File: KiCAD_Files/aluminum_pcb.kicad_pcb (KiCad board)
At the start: 2 copper layers, 160 x 133.9 mm, 189 parts, among them J1 Conn_01x01, J2 Conn_01x01, J3 Conn_01x01, J5 Conn_01x01, J8 Conn_01x01, K1 HF140FF/012-2HSWTF, Q11 NMOS, T1 Transformer_1P_1S, T2 Transformer_1P_1S, U1 INA240A1PW, U2 INA240A1PWR, U3 UCC27282DRC, U4 UCC27282DRC, U401 AMC1311BDWVR, U402 MCP6486UT-E/LT, U5 AMC1301DWR, U501 AMC1301DWR, U502 MCP6486UT-E/LT, U701 MCP6486UT-E/LT, U8 MCP6486UT-E/LT, U801 ISO7720DWV, U802 ISO7720DWV, U803 ISO7330C

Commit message: First routing pass complete.
Signed-off-by: Jean Alinei <jean.alinei@owntech.org>
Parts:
- removed C2, C4: C_Small, Capacitor_SMD:C_0805_2012Metric
- removed C5002: 470nF, Footprints:C_0805_2012Metric
- removed C5005: 4.7uF, Footprints:C_1210_3225Metric
- removed HS1, HS13, HS14, HS15, HS16, HS17, HS18, HS2, HS6, HS7, HS8: 5x3mm pad 3mm high, Footprints:BTC-533-ZN01
- removed L5001: 10uH, Inductor_SMD:L_1210_3225Metric
- added C101: 4.7uF, Capacitor_SMD:C_0805_2012Metric, F.Cu at (196.1, 88.4)
- added C102: 4.7uF, Capacitor_SMD:C_0805_2012Metric, F.Cu at (200.1, 59.5)
- added C103: 10µF, Capacitor_SMD:C_1206_3216Metric, F.Cu at (97.6, 148.1)
- added C104: C, Capacitor_SMD:C_1206_3216Metric, F.Cu at (97.6, 150.4)
- added C105: C, Capacitor_SMD:C_1206_3216Metric, F.Cu at (97.6, 152.7)
- added C106: C, Capacitor_SMD:C_1206_3216Metric, F.Cu at (97.6, 155.0)
- added C107: C, Capacitor_SMD:C_1206_3216Metric, F.Cu at (107.0, 155.0)
- added C108: C, Capacitor_SMD:C_1206_3216Metric, F.Cu at (107.0, 152.7)
- added C109: C, Capacitor_SMD:C_1206_3216Metric, F.Cu at (107.0, 150.4)
- added C110: 10µF, Capacitor_SMD:C_1206_3216Metric, F.Cu at (107.0, 148.1)
- added C111: 47uF, Capacitor_SMD:C_Elec_10x10.2, F.Cu at (96.6, 137.1)
- added C112: 47uH, Capacitor_SMD:C_Elec_10x10.2, F.Cu at (96.2, 165.2)
- added C113: ?nF, Capacitor_THT:C_Rect_L16.5mm_W7.0mm_P15.00mm_MKT, F.Cu at (142.3, 72.4)
- added C114: 1nF, Capacitor_SMD:C_1210_3225Metric, F.Cu at (210.0, 71.1)
- added C115: 1nF, Capacitor_SMD:C_1210_3225Metric, F.Cu at (210.0, 76.4)
- added C701: 1nF, Capacitor_SMD:C_0805_2012Metric, B.Cu at (86.6, 136.6)
- added C703: 100nF, Capacitor_SMD:C_0805_2012Metric, F.Cu at (137.6, 115.0)
- added C704: 22uF, Capacitor_SMD:C_1210_3225Metric, F.Cu at (123.3, 111.8)
- added C705: 33pF, Capacitor_SMD:C_0805_2012Metric, F.Cu at (134.3, 122.3)
- added C706: 10uF, Capacitor_SMD:C_0805_2012Metric, F.Cu at (120.3, 108.3)
- added C707: 100nF, Capacitor_SMD:C_0805_2012Metric, F.Cu at (117.1, 104.3)
- added C708: 47uF, Capacitor_SMD:C_1206_3216Metric, F.Cu at (119.4, 102.8)
- added C709: 10uF, Capacitor_SMD:C_0805_2012Metric, F.Cu at (140.2, 101.1)
- added C710: 10uF, Capacitor_SMD:C_0805_2012Metric, F.Cu at (109.9, 100.0)
- added C711: 10uF, Capacitor_SMD:C_0805_2012Metric, F.Cu at (143.2, 104.2)
- added C712: 10uF, Capacitor_SMD:C_0805_2012Metric, F.Cu at (111.1, 97.2)
- added C713: 100nF, Capacitor_SMD:C_0603_1608Metric, F.Cu at (146.5, 105.5)
- added C714: 100nF, Capacitor_SMD:C_0603_1608Metric, F.Cu at (109.3, 97.0)
- added C715: 10uF, Capacitor_SMD:C_0805_2012Metric, F.Cu at (161.6, 101.6)
- added C716: 10uF, Capacitor_SMD:C_0805_2012Metric, F.Cu at (106.1, 79.2)
- added C717: 470nF, Footprints:C_0805_2012Metric, F.Cu at (123.9, 115.8)
- added C718: 4.7uF, Footprints:C_1210_3225Metric, F.Cu at (126.6, 115.6)
- added C807: 100nF, Capacitor_SMD:C_0805_2012Metric, F.Cu at (200.4, 89.2)
- added C808: 100nF, Capacitor_SMD:C_0805_2012Metric, F.Cu at (199.1, 54.6)
- added C809: 100nF, Capacitor_SMD:C_0805_2012Metric, F.Cu at (214.3, 88.0)
- added D101: D, Footprints:D_SOD-123, F.Cu at (208.5, 87.6)
- added D102: D, Footprints:D_SOD-123, F.Cu at (207.7, 59.5)
- added D701: PMEG3010, Diode_SMD:D_SOD-323F, F.Cu at (161.5, 97.0)
- added D702: PMEG3010, Diode_SMD:D_SOD-323F, F.Cu at (161.4, 103.8)
- added D703: PMEG3010, Diode_SMD:D_SOD-323F, F.Cu at (103.6, 79.4)
- added D704: PMEG3010, Diode_SMD:D_SOD-323F, F.Cu at (110.3, 79.3)
- added F101: 2.5A, Footprints:FUSE-TH_L8.4-W4.1-P5.08-D0.6, F.Cu at (83.0, 79.5)
- added FL3: 1mH, Footprints:IND-TH_4P-L23.0-W15.0-P7.50-D1.0-S9.0, F.Cu at (82.0, 147.2)
- added HS101: 5x3mm pad 3mm high, Footprints:BTC-533-ZN01, B.Cu at (198.3, 148.5)
- added HS102: 5x3mm pad 3mm high, Footprints:BTC-533-ZN01, B.Cu at (179.5, 108.4)
- added HS103: 5x3mm pad 3mm high, Footprints:BTC-533-ZN01, B.Cu at (179.8, 148.3)
- added HS104: 5x3mm pad 3mm high, Footprints:BTC-533-ZN01, B.Cu at (126.9, 148.4)
- added HS105: 5x3mm pad 3mm high, Footprints:BTC-533-ZN01, B.Cu at (129.6, 171.8)
- added HS106: 5x3mm pad 3mm high, Footprints:BTC-533-ZN01, B.Cu at (129.6, 166.0)
- added HS107: 5x3mm pad 3mm high, Footprints:BTC-533-ZN01, B.Cu at (129.8, 138.6)
- added HS108: 5x3mm pad 3mm high, Footprints:BTC-533-ZN01, B.Cu at (129.8, 132.9)
- added HS109: 5x3mm pad 3mm high, Footprints:BTC-533-ZN01, B.Cu at (127.0, 156.0)
- added JP901: Jumper_2_Open, Connector_PinHeader_2.54mm:PinHeader_1x02_P2.54mm_Vertical, F.Cu at (112.1, 112.1)
- added L701: 68uH - 70mR, Inductor_SMD:L_12x12mm_H6mm, F.Cu at (132.2, 106.4)
- added L702: 4.7uH - 80mR, Inductor_SMD:L_Cenker_CKCS4020, F.Cu at (122.9, 104.5)
- added L703: 10uH, Inductor_SMD:L_0805_2012Metric, F.Cu at (143.2, 102.3)
- added L704: 10uH, Inductor_SMD:L_0805_2012Metric, F.Cu at (113.0, 97.3)
- added L705: 10uH, Inductor_SMD:L_1210_3225Metric, F.Cu at (124.4, 119.5)
- added Logo1: ~, Footprints:owntech34mmneg, B.Cu at (94.8, 167.3)
- added Logo101: ~, Footprints:owntech_mini10, F.Cu at (5.00, 0.93)
- added N101: Die cast enclosure BS11 / G124 /1550G, Footprints:Die Cast Casing 1550G, F.Cu at (162.0, 110.5)
- added R102: 3.3R, Resistor_SMD:R_0805_2012Metric, F.Cu at (204.3, 87.6)
- added R103: 3.3R, Resistor_SMD:R_0805_2012Metric, F.Cu at (203.6, 59.5)
- added R104: 20, Resistor_SMD:R_0603_1608Metric, B.Cu at (124.8, 140.1)
- added R105: 20, Resistor_SMD:R_0603_1608Metric, B.Cu at (125.4, 143.4)
- added R106: 20, Resistor_SMD:R_0603_1608Metric, B.Cu at (123.9, 167.8)
- added R107: 20, Resistor_SMD:R_0603_1608Metric, B.Cu at (127.6, 159.7)
- added R108: 20, Resistor_SMD:R_0603_1608Metric, B.Cu at (124.8, 133.8)
- added R109: 20k, Resistor_SMD:R_0603_1608Metric, B.Cu at (124.8, 173.0)
- added R701: 110k, Footprints:R_0805_2012Metric, F.Cu at (134.3, 124.3)
- added R702: 10k, Footprints:R_0805_2012Metric, F.Cu at (134.3, 120.4)
- added R703: 65k, Footprints:R_0805_2012Metric, F.Cu at (130.1, 120.3)
- added R704: 100k, Footprints:R_0805_2012Metric, F.Cu at (137.6, 118.6)
- added R705: 56k, Footprints:R_0805_2012Metric, F.Cu at (115.1, 105.5)
- added R706: 10k, Footprints:R_0805_2012Metric, F.Cu at (116.9, 108.3)
- added R707: 4.7k, Resistor_SMD:R_0603_1608Metric, F.Cu at (161.5, 99.8)
- added R708: 4.7k, Resistor_SMD:R_0603_1608Metric, F.Cu at (108.1, 79.4)
- added R801: 10k, Capacitor_SMD:C_0805_2012Metric, F.Cu at (199.3, 92.2)
- added R802: 10k, Capacitor_SMD:C_0805_2012Metric, F.Cu at (201.3, 92.2)
- added R803: 1k, Capacitor_SMD:C_0805_2012Metric, F.Cu at (196.1, 90.4)
- added R804: 1k, Capacitor_SMD:C_0805_2012Metric, F.Cu at (200.1, 57.4)
- added R805: 10k, Capacitor_SMD:C_0805_2012Metric, F.Cu at (196.0, 57.3)
- added R806: 10k, Capacitor_SMD:C_0805_2012Metric, F.Cu at (196.0, 59.4)
- added R807: 470, Capacitor_SMD:C_0805_2012Metric, F.Cu at (213.5, 90.7)
- added R808: 10k, Capacitor_SMD:C_0805_2012Metric, F.Cu at (213.4, 92.7)
- added R809: 10k, Capacitor_SMD:C_0805_2012Metric, F.Cu at (210.7, 92.0)
- added R901: 27k, Footprints:R_0805_2012Metric, F.Cu at (112.0, 109.3)
- added RV101: TMOV14RP275, Varistor:RV_Disc_D12mm_W6.2mm_P7.5mm, F.Cu at (133.6, 51.6)
- added RV102: TMOV14RP275, Varistor:RV_Disc_D12mm_W6.2mm_P7.5mm, F.Cu at (148.4, 78.3)
- added RV103: TMOV14RP275, Varistor:RV_Disc_D12mm_W6.2mm_P7.5mm, F.Cu at (164.9, 70.5)
- added TR701: VPT87DDF01B, Footprints:VPT87BB-01B, F.Cu at (152.5, 100.3)
- added TR702: VPT87DFB01B, Footprints:VPT87BB-01B, F.Cu at (106.9, 88.5)
- added U702: TPS562202, Package_TO_SOT_SMD:SOT-563, F.Cu at (119.3, 106.2)
- added U703: VPS8701B, Package_TO_SOT_SMD:SOT-23-6, F.Cu at (143.3, 99.7)
- added U704: VPS8701B, Package_TO_SOT_SMD:SOT-23-6, F.Cu at (106.2, 97.7)
- added U707: LMR38020SDDAR, Package_SO:Texas_HSOP-8-1EP_3.9x4.9mm_P1.27mm_ThermalVias, F.Cu at (132.2, 116.6)
- added U804: TL431DBZ, Package_TO_SOT_SMD:SOT-23, F.Cu at (196.2, 93.2)
- added U805: TL431, Package_TO_SOT_SMD:SOT-23, F.Cu at (196.3, 54.3)
- added U806: TL431, Package_TO_SOT_SMD:SOT-23, F.Cu at (211.6, 95.5)
- added U901: OwnTech_SPIN, Footprints:OwnTech_SPINTHT_1, F.Cu at (107.6, 124.5)
- C22, C27, C33, C38: footprint Capacitor_THT:C_Rect_L16.5mm_W8.7mm_P15.00mm_MKT -> Footprints:C_Rect_L16.5mm_W8mm_P15.00mm_MKT
- C28, C401, C402, C403, C702, C801, C802, C803, C804, R3, Rv401, Rv402, Rv403, Rv404, Rv405, Rv501, Rv502, Rv503, Rv504, Rv505, Rv701, Rv702, U1, U2, U401, U701: moved to B.Cu
- C39: footprint Capacitor_SMD:C_1206_3216Metric -> Capacitor_SMD:C_0805_2012Metric; moved to B.Cu
- D5: value D_Schottky -> 40V - BAT165E6327F; footprint Diode_SMD:D_SMA -> Diode_SMD:D_SOD-323
- F1: value T5A250V -> 2.5A
- Q1, Q2, Q3, Q4: value ~ -> CID12N65D
- Q10, Q5, Q6, Q7, Q8, Q9: value ~ -> CJAC90SN12
- Q11: value NMOS -> ZXMN7A11GTA
- R101, R32, R33, R6, R8, R9: footprint Resistor_SMD:R_0805_2012Metric -> Resistor_SMD:R_0603_1608Metric; moved to B.Cu
- Rv14: footprint Resistor_SMD:R_0805_2012Metric -> Resistor_SMD:R_2512_6332Metric
- U801, U802: value ISO7720DWV -> ISO7720FDR; footprint Package_SO:SOIC-8_7.5x5.85mm_P1.27mm -> Package_SO:SOIC-8_3.9x4.9mm_P1.27mm; moved to B.Cu
- U803: value ISO7330C -> ISO7720FDR; footprint Package_SO:SOIC-16W_7.5x10.3mm_P1.27mm -> Package_SO:SOIC-8_3.9x4.9mm_P1.27mm
- moved U803 197.5 mm to (151.0, 92.2), turned to 15 degrees
- moved C805 195.3 mm to (146.3, 93.4), turned to 105 degrees
- moved C806 193.5 mm to (156.0, 90.8), turned to 105 degrees
- moved C803 192.0 mm to (144.7, 88.5), turned to -75 degrees
- moved U802 191.0 mm to (149.6, 87.0), turned to 15 degrees
- moved C804 189.8 mm to (154.4, 85.9), turned to -75 degrees
- moved C801 181.6 mm to (146.0, 93.5), turned to -75 degrees
- moved U801 180.4 mm to (151.0, 92.3), turned to 15 degrees
- moved C802 179.4 mm to (156.0, 90.9), turned to -75 degrees
- moved Rv401 174.3 mm to (178.2, 101.0), turned to 170 degrees
- moved Rv403 173.0 mm to (171.5, 99.8), turned to 170 degrees
- moved Rv402 172.4 mm to (174.9, 100.4), turned to 170 degrees
- moved C404 171.6 mm to (136.8, 105.0)
- moved R404 171.6 mm to (136.7, 103.1)
- moved U402 171.4 mm to (136.7, 100.8)
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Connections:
- net /Power/EN_{I} renamed /Microcontroller/EN_{I}
- net /Power/Relay renamed /Microcontroller/Relay
- net /Power/V_{DCBus} renamed /Microcontroller/V_{DCBus}
- C1 pad 2: /Power/SN2 -> /SN2
- C18 pad 2: Net-(T1-AB) -> Net-(C18-Pad2)
- C19 pad 2: Net-(T1-AB) -> Net-(C18-Pad2)
- C20 pad 2: Net-(T1-AB) -> Net-(C18-Pad2)
- C21 pad 2: Net-(T1-AB) -> Net-(C18-Pad2)
- C23 pad 1: Net-(T1-AB) -> Net-(C18-Pad2)
- C23 pad 2: GND_{LV} -> DGND
- C24 pad 1: Net-(T1-AB) -> Net-(C18-Pad2)
- C24 pad 2: GND_{LV} -> DGND
- C25 pad 1: Net-(T1-AB) -> Net-(C18-Pad2)
- C25 pad 2: GND_{LV} -> DGND
- C26 pad 1: Net-(T1-AB) -> Net-(C18-Pad2)
- C26 pad 2: GND_{LV} -> DGND
- C28 pad 1: +5V_{LV} -> +5V_{DGND}
- C28 pad 2: GND_{LV} -> DGND
- C29 pad 2: Net-(T2-AB) -> Net-(C29-Pad2)
- C3 pad 2: /Power/SN1 -> /SN1
- C30 pad 2: Net-(T2-AB) -> Net-(C29-Pad2)
- C31 pad 2: Net-(T2-AB) -> Net-(C29-Pad2)
- C32 pad 2: Net-(T2-AB) -> Net-(C29-Pad2)
- C34 pad 1: Net-(T2-AB) -> Net-(C29-Pad2)
- C34 pad 2: GND_{LV} -> DGND
- C35 pad 1: Net-(T2-AB) -> Net-(C29-Pad2)
- C35 pad 2: GND_{LV} -> DGND
- C36 pad 1: Net-(T2-AB) -> Net-(C29-Pad2)
- C36 pad 2: GND_{LV} -> DGND
- C37 pad 1: Net-(T2-AB) -> Net-(C29-Pad2)
- C37 pad 2: GND_{LV} -> DGND
- C39 pad 1: +5V_{LV} -> +5V_{DGND}
- C39 pad 2: GND_{LV} -> DGND
- C40 pad 2: /Power/HS1 -> /Power/LSW1
- C402 pad 2: +5V_{IGND} -> +5V_{HV}
- C53 pad 1: +12V_{LV} -> +12V_{DGND}
- C53 pad 2: GND_{LV} -> DGND
- C8 pad 2: /Power/HS2 -> /Power/LSW2
- C802 pad 1: /Power/SN1 -> /SN1
- C804 pad 1: /Power/SN2 -> /SN2
- C9 pad 1: +12V_{LV} -> +12V_{DGND}
- C9 pad 2: GND_{LV} -> DGND
- D1 pad 2: Net-(D1-A) -> /Power/Rect1
- D2 pad 1: Net-(D1-A) -> /Power/Rect1
- D3 pad 2: Net-(D3-A) -> /Power/Rect2
- D4 pad 1: Net-(D3-A) -> /Power/Rect2
- FB1 pad 1: /Power/SN2 -> /SN2
- FB2 pad 1: /Power/SN1 -> /SN1
- FL1 pad 3: Net-(FL1-Pad3) -> Net-(C113-Pad2)
- FL2 pad 3: Net-(C10-Pad2) -> /Power/AC Current sense/In-
- FL2 pad 4: /Power/AC Current sense/In- -> Net-(C10-Pad2)
- HS10 pad 1: Net-(HS10-Pad1) -> GND_{HV}
- HS11 pad 1: Net-(HS11-Pad1) -> /Power/Rect1
- HS12 pad 1: Net-(HS11-Pad1) -> /Power/Rect2
- HS3 pad 1: Net-(HS3-Pad1) -> /SN1
- HS4 pad 1: Net-(HS10-Pad1) -> /SN2
- HS5 pad 1: Net-(HS11-Pad1) -> /Power/HV_{BUS}
- HS9 pad 1: Net-(HS10-Pad1) -> GND_{HV}
- J2 pad 1: /Power/AC Current sense/In+ -> Net-(J2-Pin_1)
- J3 pad 1: Earth -> Earth_Protective
- K1 pad 6: Net-(FL1-Pad4) -> Net-(C113-Pad2)
- L3 pad 2: Net-(FL1-Pad3) -> Net-(FL1-Pad4)
- L5 pad 2: /Power/HS1 -> /Power/LSW1
- L6 pad 2: /Power/HS2 -> /Power/LSW2
- Q1 pad 11: /Power/SN2 -> /SN2
- Q1 pad 12: /Power/SN2 -> /SN2
- Q1 pad 7: /Power/SN2 -> /SN2
- Q10 pad 1: GND_{LV} -> DGND
- Q10 pad 2: /Power/LO2 -> Net-(Q10-G)
- Q10 pad 3: /Power/HS2 -> /Power/LSW2
- Q11 pad 1: Net-(D5-A) -> Net-(Q11-G)
- Q11 pad 2: Net-(Q11-G) -> Net-(D5-A)
- Q11 pad 4: (no net) -> Net-(D5-A)
- Q2 pad 11: /Power/SN1 -> /SN1
- Q2 pad 12: /Power/SN1 -> /SN1
- Q2 pad 7: /Power/SN1 -> /SN1
- Q3 pad 1: /Power/SN1 -> /SN1
- Q4 pad 1: /Power/SN2 -> /SN2
- Q5 pad 1: /Power/HS1 -> /Power/LSW1
- Q5 pad 2: /Power/HO1 -> Net-(Q5-G)
- Q6 pad 1: GND_{LV} -> DGND
- Q6 pad 2: /Power/LO1 -> Net-(Q6-G)
- Q6 pad 3: /Power/HS1 -> /Power/LSW1
- Q7 pad 1: GND_{LV} -> DGND
- Q7 pad 2: /Power/LO1 -> Net-(Q7-G)
- Q7 pad 3: /Power/HS1 -> /Power/LSW1
- Q8 pad 1: /Power/HS2 -> /Power/LSW2
- Q8 pad 2: /Power/HO2 -> Net-(Q8-G)
- Q9 pad 1: GND_{LV} -> DGND
- Q9 pad 2: /Power/LO2 -> Net-(Q9-G)
- Q9 pad 3: /Power/HS2 -> /Power/LSW2
- R101 pad 1: GND_{LV} -> DGND
- R101 pad 2: /Power/LO2 -> Net-(Q10-G)
- R3 pad 2: Net-(FL1-Pad3) -> Net-(FL1-Pad4)
- R32 pad 1: GND_{LV} -> DGND
- R32 pad 2: /Power/LO1 -> Net-(Q6-G)
- R33 pad 1: GND_{LV} -> DGND
- R33 pad 2: /Power/LO2 -> Net-(Q9-G)
- R6 pad 1: /Power/HS1 -> /Power/LSW1
- R6 pad 2: /Power/HO1 -> Net-(Q5-G)
- R8 pad 1: GND_{LV} -> DGND
- R8 pad 2: /Power/LO1 -> Net-(Q7-G)
- R9 pad 1: /Power/HS2 -> /Power/LSW2
- R9 pad 2: /Power/HO2 -> Net-(Q8-G)
- Rv702 pad 2: GND_{LV} -> DGND
- T1 pad 1: /Power/HS1 -> (no net)
- T1 pad 2: Net-(T1-AB) -> /Power/Rect1
- T1 pad 3: Net-(T1-SA) -> (no net)
- T2 pad 1: /Power/HS2 -> (no net)
- T2 pad 2: Net-(T2-AB) -> /Power/Rect2
- T2 pad 3: Net-(T2-SA) -> (no net)
- U1 pad 1: GND_{LV} -> DGND
- U1 pad 4: GND_{LV} -> DGND
- U1 pad 5: +5V_{LV} -> +5V_{DGND}
- U1 pad 6: GND_{LV} -> DGND
- U1 pad 7: GND_{LV} -> DGND
- U1 pad 8: /Power/I_{ILow1} -> /Microcontroller/I_{ILow1}
- U2 pad 1: GND_{LV} -> DGND
- U2 pad 4: GND_{LV} -> DGND
- U2 pad 5: +5V_{LV} -> +5V_{DGND}
- U2 pad 6: GND_{LV} -> DGND
- U2 pad 7: GND_{LV} -> DGND
- U2 pad 8: /Power/I_{ILow2} -> /Microcontroller/I_{ILow2}
- U3 pad 1: +12V_{LV} -> +12V_{DGND}
- U3 pad 11: GND_{LV} -> DGND
- U3 pad 5: /Power/HS1 -> /Power/LSW1
- U3 pad 7: /Power/PWM_{IHigh1} -> /Microcontroller/PWM_{IHigh1}
- U3 pad 8: /Power/PWM_{ILow1} -> /Microcontroller/PWM_{ILow1}
- U3 pad 9: GND_{LV} -> DGND
- U4 pad 1: +12V_{LV} -> +12V_{DGND}
- U4 pad 11: GND_{LV} -> DGND
- U4 pad 5: /Power/HS2 -> /Power/LSW2
- U4 pad 7: /Power/PWM_{IHigh2} -> /Microcontroller/PWM_{IHigh2}
- U4 pad 8: /Power/PWM_{ILow2} -> /Microcontroller/PWM_{ILow2}
- U4 pad 9: GND_{LV} -> DGND
- U401 pad 1: +5V_{IGND} -> +5V_{HV}
- U801 pad 2: /Signal Isolators/IN1_{SN1} -> /Microcontroller/PWM_{IIHigh1}
- U801 pad 3: /Signal Isolators/IN2_{SN1} -> unconnected-(U801-INB-Pad3)
- U801 pad 5: /Power/SN1 -> /SN1
- U801 pad 6: /Power/EN_{SN1} -> unconnected-(U801-OUTB-Pad6)
- U802 pad 2: /Signal Isolators/IN1_{SN2} -> /Microcontroller/PWM_{IIHigh2}
- U802 pad 3: /Signal Isolators/IN2_{SN1} -> unconnected-(U802-INB-Pad3)
- U802 pad 5: /Power/SN2 -> /SN2
- U802 pad 6: /Power/EN_{SN2} -> unconnected-(U802-OUTB-Pad6)
- U803 pad 2: DGND -> /Microcontroller/PWM_{IILow1}
- U803 pad 3: /Signal Isolators/IN1_{GNDHV} -> /Microcontroller/PWM_{IILow2}
- U803 pad 4: /Signal Isolators/IN2_{GNDHV} -> DGND
- U803 pad 5: /Signal Isolators/IN2_{SN1} -> GND_{HV}
- U803 pad 6: unconnected-(U803-NC-Pad6) -> /Power/PWM_{IILow2}
- U803 pad 7: unconnected-(U803-NC-Pad7) -> /Power/PWM_{IILow1}
- U803 pad 8: DGND -> +5V_{HV}
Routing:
- net +5V_{DGND}: track 0.00 -> 275.7 mm, vias 0 -> 15
- net +12V_{DGND}: track 0.00 -> 182.0 mm, vias 0 -> 13
- net +5V_{HV}: track 0.00 -> 156.8 mm, vias 0 -> 2
- net +12V_{HV}: track 0.00 -> 138.0 mm
- net /Microcontroller/EN_{I}: track 0.00 -> 121.8 mm, vias 0 -> 2
- net /Microcontroller/PWM_{IHigh2}: track 0.00 -> 112.8 mm, vias 0 -> 1
- net /Microcontroller/PWM_{ILow2}: track 0.00 -> 107.9 mm, vias 0 -> 1
- net /Microcontroller/PWM_{IILow1}: track 0.00 -> 100.4 mm, vias 0 -> 2
- net /Microcontroller/PWM_{IIHigh1}: track 0.00 -> 100.3 mm
- net /Microcontroller/I_{ILow2}: track 0.00 -> 99.0 mm
- net /Microcontroller/PWM_{IIHigh2}: track 0.00 -> 89.8 mm, vias 0 -> 1
- net /Power/V_{ILow}: track 0.00 -> 87.5 mm, vias 0 -> 2
- net /Microcontroller/PWM_{IILow2}: track 0.00 -> 84.7 mm, vias 0 -> 2
- net /Microcontroller/I_{ILow1}: track 0.00 -> 76.2 mm, vias 0 -> 1
- net /Power/PWM_{IILow1}: track 0.00 -> 74.2 mm, vias 0 -> 2
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- added copper zone on F.Cu, net +12V_{DGND}
- added copper zone on F.Cu, net +12V_{HV}
- added copper zone on F.Cu, net +5V_{ACsense}
- added copper zone on F.Cu, net +5V_{DGND}
- added copper zone on F.Cu, net +5V_{SN1}
- added copper zone on F.Cu, net +5V_{SN2}
- added copper zone on In1.Cu, net /Power/AC Current sense/In-
- added copper zone on F.Cu, net /Power/HV_{BUS}
- added copper zone on B.Cu, net /Power/LSW1
- added copper zone on F.Cu, net /Power/LSW1
- added copper zone on F.Cu, net /Power/LSW2
- added copper zone on B.Cu, net /Power/Rect1
- added copper zone on F.Cu, net /Power/Rect1
- added copper zone on B.Cu, net /Power/Rect2
- added copper zone on F.Cu, net /Power/Rect2
- added copper zone on F.Cu, net /Power/V_{IHigh1}
- added copper zone on F.Cu, net /Power/V_{IHigh2}
- added copper zone on F.Cu, net /Power/V_{ILow}
- added copper zone on F.Cu, net /SN1
- added copper zone on F.Cu, net /SN2
- added copper zone on B.Cu, net DGND
- added copper zone on F.Cu, net DGND
- added copper zone on In1.Cu, net DGND
- added copper zone on In2.Cu, net DGND
- added copper zone on B.Cu, net Earth_Protective
- added copper zone on F.Cu, net Earth_Protective
- added copper zone on B.Cu, net GND_{HV}
- added copper zone on F.Cu, net GND_{HV}
- added copper zone on In1.Cu, net GND_{HV}
- added copper zone on In2.Cu, net GND_{HV}
- added copper zone on F.Cu, net Net-(C18-Pad2)
- added copper zone on F.Cu, net Net-(C29-Pad2)
- added copper zone on F.Cu, net Net-(C7-Pad1)
- added copper zone on B.Cu, net Net-(C7-Pad2)
- added copper zone on F.Cu, net Net-(C716-Pad2)
- added copper zone on F.Cu, net Net-(D5-A)
- added copper zone on F.Cu, net Net-(D701-A)
- added copper zone on F.Cu, net Net-(D702-A)
- added copper zone on F.Cu, net Net-(D703-A)
- added copper zone on F.Cu, net Net-(D704-A)
- added copper zone on F.Cu, net Net-(FB1-Pad2)
- added copper zone on F.Cu, net Net-(FB2-Pad2)
- added copper zone on B.Cu, net Net-(FL1-Pad4)
- added copper zone on F.Cu, net Net-(GD1-Pad3)
- added copper zone on F.Cu, net Net-(J1-Pin_1)
- added copper zone on F.Cu, net Net-(J2-Pin_1)
- added copper zone on B.Cu, net Net-(J5-Pin_1)
- added copper zone on F.Cu, net Net-(J5-Pin_1)
- added copper zone on F.Cu, net Net-(J8-Pin_1)
- added copper zone on B.Cu, net Net-(T1-SA)
- added copper zone on B.Cu, net Net-(T2-SA)
- added copper zone on F.Cu, net Net-(U1-+)
- added copper zone on F.Cu, net Net-(U2-+)
- added copper zone on F.Cu, net Net-(U702-SW)
- added copper zone on F.Cu, net Net-(U703-VD1)
- added copper zone on F.Cu, net Net-(U703-VD2)
- added copper zone on F.Cu, net Net-(U703-VIN)
- added copper zone on F.Cu, net Net-(U704-VD1)
- added copper zone on F.Cu, net Net-(U704-VD2)
- added copper zone on F.Cu, net Net-(U704-VIN)
- added copper zone on F.Cu, net Net-(U707-EN)
- added copper zone on F.Cu, net Net-(U707-SW)
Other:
- board size 160 x 133.9 mm -> 178.9 x 131.8 mm
- copper layers 2 -> 4

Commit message: Added missing tracks for sensors and relay. Fixed many routing issues.
Signed-off-by: Jean Alinei <jean.alinei@owntech.org>
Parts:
- removed HS102, HS103: 5x3mm pad 3mm high, Footprints:BTC-533-ZN01
- added HS110: 5x3mm pad 3mm high, Footprints:BTC-533-ZN01, B.Cu at (107.6, 137.3)
- added HS111: 5x3mm pad 3mm high, Footprints:BTC-533-ZN01, B.Cu at (107.8, 165.2)
- moved Logo1 8.40 mm to (86.6, 165.2)
- moved HS5 0.60 mm to (197.8, 108.0)
- moved HS11 0.10 mm to (187.3, 108.0)
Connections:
- net Net-(U1-+) renamed /Power/ThPad_{IND1}
- net Net-(U2-+) renamed /Power/ThPad_{IND2}
- C43 pad 2: /Power/AC Current sense/I_{ACsense} -> /Microcontroller/V_{AC}
- C47 pad 1: /Power/AC Current sense/In- -> /Feeder/Neut_{REF}
- C502 pad 1: /Power/AC Current sense/In- -> /Feeder/Neut_{REF}
- C504 pad 2: /Power/Grid Voltage sense/V_{ACsense} -> /Microcontroller/I_{AC}
- C716 pad 2: Net-(C716-Pad2) -> /Feeder/Neut_{REF}
- FL2 pad 3: /Power/AC Current sense/In- -> /Feeder/Neut_{REF}
- R17 pad 2: /Power/AC Current sense/I_{ACsense} -> /Microcontroller/V_{AC}
- R504 pad 2: /Power/Grid Voltage sense/V_{ACsense} -> /Microcontroller/I_{AC}
- R708 pad 2: Net-(C716-Pad2) -> /Feeder/Neut_{REF}
- Rv14 pad 2: /Power/AC Current sense/In- -> /Feeder/Neut_{REF}
- Rv16 pad 1: /Power/AC Current sense/In- -> /Feeder/Neut_{REF}
- Rv505 pad 2: /Power/AC Current sense/In- -> /Feeder/Neut_{REF}
- Rv507 pad 1: /Power/AC Current sense/In- -> /Feeder/Neut_{REF}
- TR702 pad 6: Net-(C716-Pad2) -> /Feeder/Neut_{REF}
- TR702 pad 7: Net-(C716-Pad2) -> /Feeder/Neut_{REF}
- U5 pad 4: /Power/AC Current sense/In- -> /Feeder/Neut_{REF}
- U501 pad 4: /Power/AC Current sense/In- -> /Feeder/Neut_{REF}
- U502 pad 4: /Power/Grid Voltage sense/V_{ACsense} -> /Microcontroller/I_{AC}
- U8 pad 4: /Power/AC Current sense/I_{ACsense} -> /Microcontroller/V_{AC}
- U901 pad 19: unconnected-(U901A-PC12-Pad19) -> /Microcontroller/EN_{I}
- U901 pad 21: unconnected-(U901A-PB9-Pad21)_1 -> /Feeder/DIS_{HV}
- U901 pad 22: unconnected-(U901A-PC13-Pad22) -> /Microcontroller/Relay
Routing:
- net /Microcontroller/EN_{I}: track 121.8 -> 60.5 mm
- net /Feeder/Neut_{REF}: track 0.00 -> 50.4 mm, vias 0 -> 7
- net /Power/AC Current sense/In-: track 49.3 -> 0.00 mm, vias 3 -> 0
- net /Feeder/DIS_{HV}: track 0.00 -> 39.2 mm, vias 0 -> 1
- net /Microcontroller/Relay: track 0.00 -> 29.2 mm
- net /Microcontroller/V_{AC}: track 0.00 -> 15.8 mm, vias 0 -> 1
- net /Microcontroller/I_{AC}: track 0.00 -> 15.2 mm, vias 0 -> 1
- net /Power/AC Current sense/I_{ACsense}: track 5.08 -> 0.00 mm
- net /Power/Grid Voltage sense/V_{ACsense}: track 4.79 -> 0.00 mm
- net +5V_{DGND}: track 275.7 -> 279.3 mm, vias 15 -> 16
- net /Microcontroller/I_{ILow2}: track 99.0 -> 102.4 mm
- net /Microcontroller/I_{ILow1}: track 76.2 -> 79.3 mm
- net /Microcontroller/PWM_{IILow2}: track 84.7 -> 87.4 mm
- net /Power/V_{ILow}: track 87.5 -> 89.8 mm
- net /Power/AC Current sense/In+: track 41.1 -> 43.3 mm, vias 1 -> 3
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- added copper zone on F.Cu, net /Feeder/Neut_{REF}
- added copper zone on In1.Cu, net /Feeder/Neut_{REF}
- added copper zone on In2.Cu, net /Power/LSW1
- added copper zone on In2.Cu, net /Power/Rect1
- added copper zone on In2.Cu, net /Power/Rect2
- added copper zone on In2.Cu, net Net-(T1-SA)
- added copper zone on In2.Cu, net Net-(T2-SA)
- removed copper zone on In1.Cu, net /Power/AC Current sense/In-
- removed copper zone on B.Cu, net /Power/LSW1
- removed copper zone on B.Cu, net /Power/Rect1
- removed copper zone on B.Cu, net /Power/Rect2
- removed copper zone on F.Cu, net Net-(C716-Pad2)
- removed copper zone on B.Cu, net Net-(T1-SA)
- removed copper zone on B.Cu, net Net-(T2-SA)

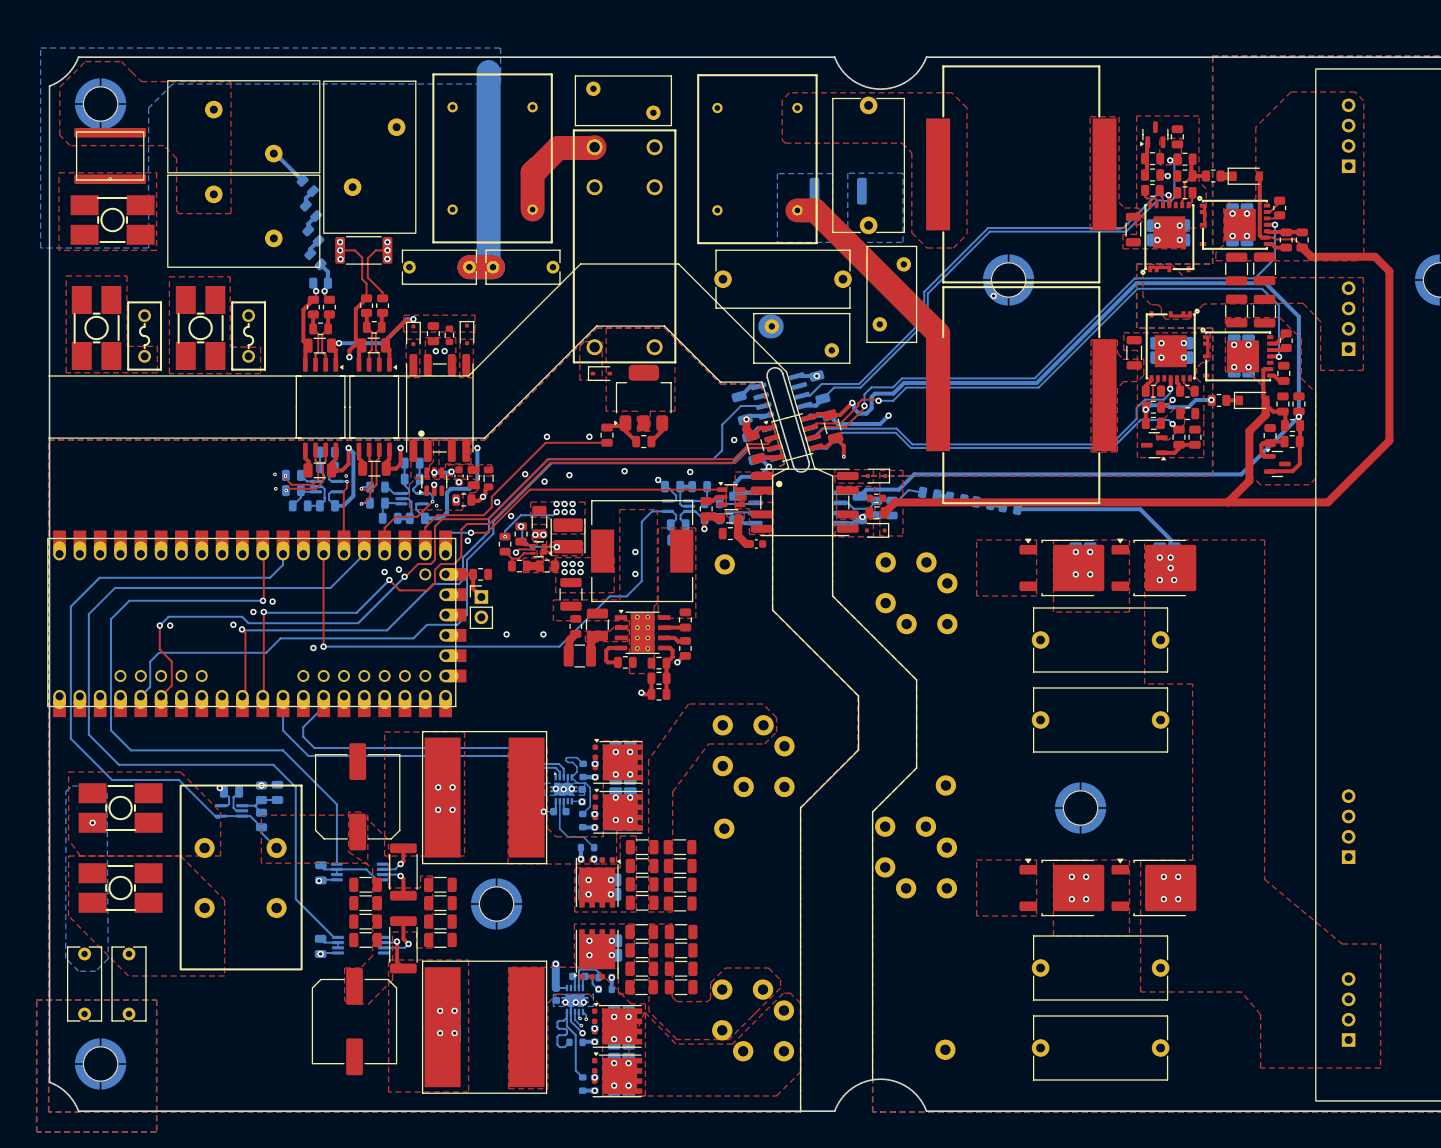
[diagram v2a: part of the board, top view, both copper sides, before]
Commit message: Added DRC rules according to IEC60664 and IPC2221.
Signed-off-by: Jean Alinei <jean.alinei@owntech.org>
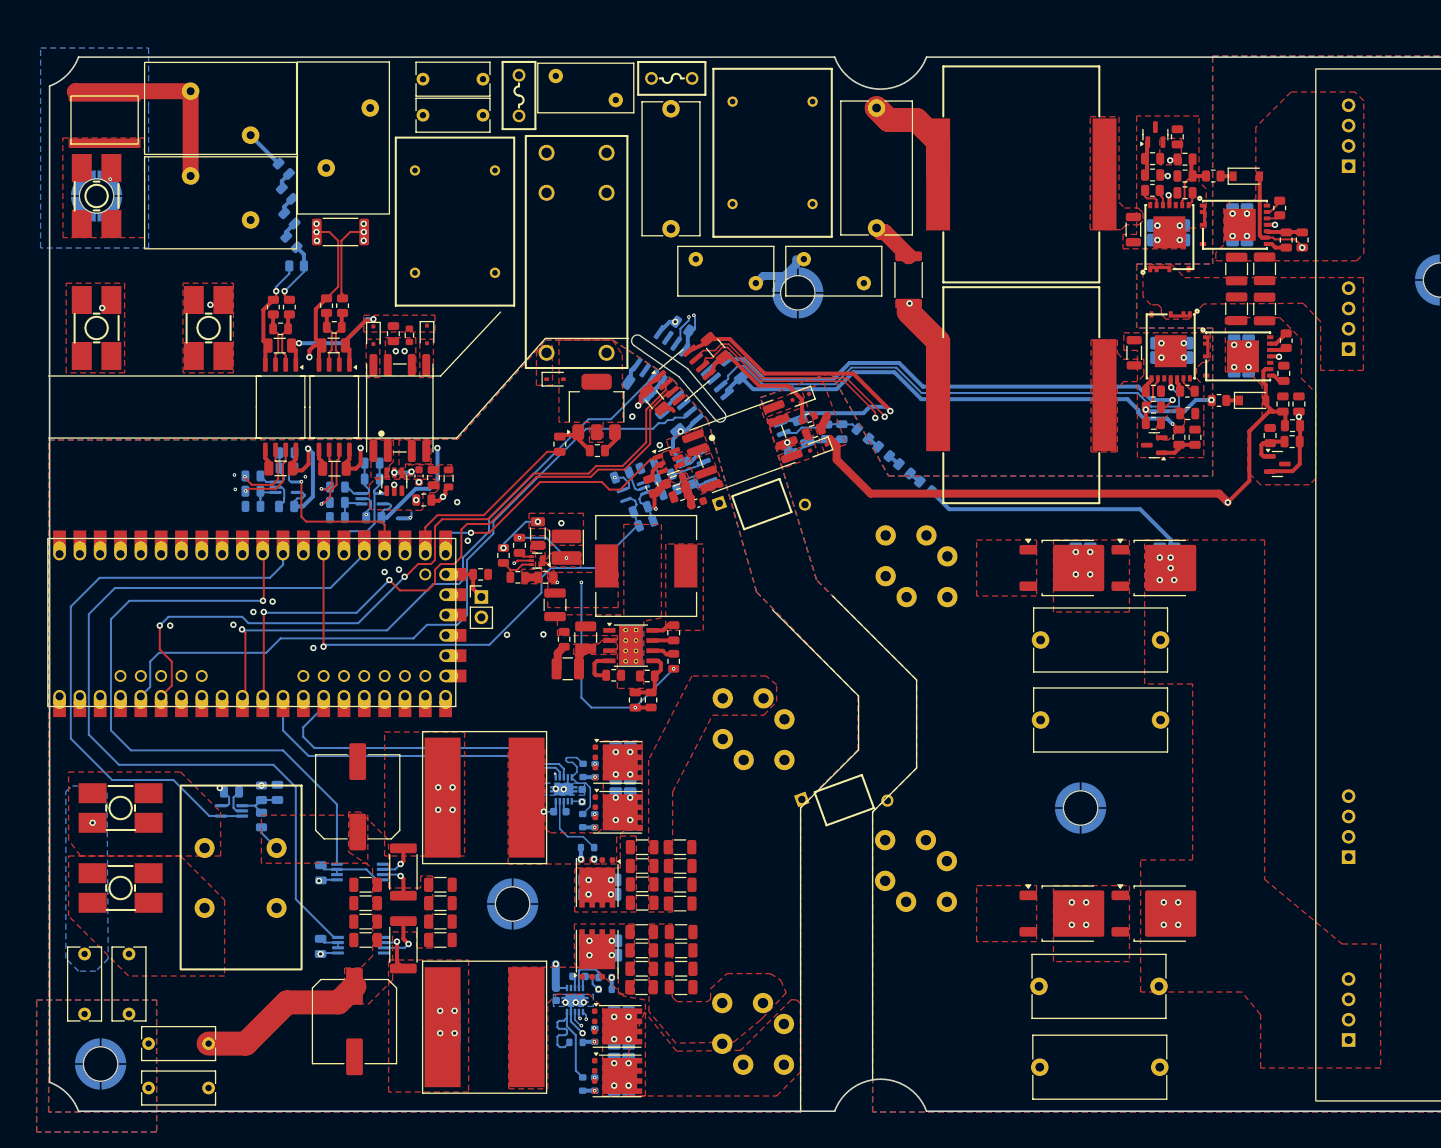
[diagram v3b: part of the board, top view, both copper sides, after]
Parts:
- added C116: 2.2nF, Capacitor_THT:C_Rect_L9.0mm_W4.0mm_P7.50mm_MKT, F.Cu at (70.5, 167.9)
- added C117: 2.2nF, Capacitor_THT:C_Rect_L9.0mm_W4.0mm_P7.50mm_MKT, F.Cu at (70.5, 173.5)
- added C118: 1nF, Footprints:CAP-TH_L6.3-W4.4-P10.00-D0.6-S3.8, F.Cu at (147.2, 100.5)
- added C119: 1nF, Footprints:CAP-TH_L6.3-W4.4-P10.00-D0.6-S3.8, F.Cu at (157.5, 137.5)
- C804: footprint Capacitor_SMD:C_1206_3216Metric -> Capacitor_SMD:C_0805_2012Metric
- R3: moved to F.Cu
- moved F1 73.3 mm to (135.9, 47.3), turned to 0 degrees
- moved F101 45.2 mm to (116.8, 49.4)
- moved H2 26.4 mm to (151.7, 74.1)
- moved RV103 26.0 mm to (138.9, 69.9), turned to 0 degrees
- moved C10 24.2 mm to (104.8, 47.4), turned to 0 degrees
- moved C113 22.3 mm to (135.8, 51.1), turned to -90 degrees
- moved C5 20.9 mm to (112.3, 51.9)
- moved C804 18.8 mm to (137.3, 78.3), turned to -35 degrees
- moved C806 17.6 mm to (141.4, 81.0), turned to 130 degrees
- moved U802 15.9 mm to (134.5, 82.1), turned to 55 degrees
- moved U803 15.6 mm to (137.5, 84.4), turned to 40 degrees
- moved C802 14.4 mm to (143.6, 83.5), turned to -50 degrees
- moved R3 14.2 mm to (165.5, 72.5), turned to -90 degrees
- moved C805 13.9 mm to (133.7, 87.4), turned to 130 degrees
- moved D701 13.7 mm to (152.0, 87.1), turned to -160 degrees
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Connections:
- net Net-(C18-Pad2) renamed /Power/LSW4
- net Net-(C29-Pad2) renamed /Power/LSW3
- C43 pad 2: /Microcontroller/V_{AC} -> /Microcontroller/I_{AC}
- C504 pad 2: /Microcontroller/I_{AC} -> /Microcontroller/V_{AC}
- F1 pad 1: /Power/Grid Voltage sense/In+ -> Net-(F1-Pad1)
- F1 pad 2: Net-(J1-Pin_1) -> Net-(C113-Pad1)
- F101 pad 1: /Power/AC Current sense/In+ -> Net-(F101-Pad1)
- F101 pad 2: Net-(J2-Pin_1) -> Net-(C113-Pad2)
- FL1 pad 2: Net-(C113-Pad1) -> Net-(F1-Pad1)
- FL1 pad 3: Net-(C113-Pad2) -> Net-(F101-Pad1)
- J1 pad 1: Net-(J1-Pin_1) -> /Power/Grid Voltage sense/In+
- J2 pad 1: Net-(J2-Pin_1) -> /Power/AC Current sense/In+
- Q1 pad 4: (no net) -> /Power/HV_{BUS}
- Q2 pad 4: (no net) -> /Power/HV_{BUS}
- Q3 pad 4: (no net) -> /SN1
- Q4 pad 4: (no net) -> /SN2
- R17 pad 2: /Microcontroller/V_{AC} -> /Microcontroller/I_{AC}
- R504 pad 2: /Microcontroller/I_{AC} -> /Microcontroller/V_{AC}
- RV101 pad 1: Net-(C113-Pad1) -> Net-(F1-Pad1)
- RV101 pad 2: Net-(C113-Pad2) -> Net-(F101-Pad1)
- U502 pad 4: /Microcontroller/I_{AC} -> /Microcontroller/V_{AC}
- U701 pad 3: /Power/V_{ILow} -> /Microcontroller/V_{ILow}
- U701 pad 4: /Power/V_{ILow} -> /Microcontroller/V_{ILow}
- U8 pad 4: /Microcontroller/V_{AC} -> /Microcontroller/I_{AC}
- U901 pad 29: /Power/V_{ILow} -> /Microcontroller/V_{ILow}
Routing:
- net /Microcontroller/V_{ILow}: track 0.00 -> 72.0 mm
- net /Power/V_{ILow}: track 89.8 -> 35.9 mm
- net Net-(F101-Pad1): track 0.00 -> 33.4 mm
- net +5V_{HV}: track 156.8 -> 126.9 mm
- net Net-(C113-Pad2): track 63.1 -> 33.6 mm
- net Net-(GD1-Pad3): track 0.00 -> 25.1 mm
- net /SN2: track 60.4 -> 85.4 mm
- net /Power/PWM_{IIHigh2}: track 59.5 -> 83.9 mm, vias 1 -> 2
- net Net-(F1-Pad1): track 0.00 -> 23.3 mm
- net +5V_{SN2}: track 64.8 -> 87.8 mm, vias 1 -> 2
- net Net-(C7-Pad1): track 0.00 -> 21.9 mm
- net /Power/PWM_{IILow1}: track 74.2 -> 92.5 mm
- net /Power/PWM_{IILow2}: track 73.0 -> 90.3 mm
- net Net-(C5-Pad1): track 45.1 -> 28.0 mm
- net /Power/PWM_{IIHigh1}: track 51.3 -> 66.4 mm
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- added copper zone on F.Cu, net /Power/AC Current sense/In+
- added copper zone on F.Cu, net /Power/Grid Voltage sense/In+
- removed copper zone on F.Cu, net Net-(C7-Pad1)
- removed copper zone on B.Cu, net Net-(C7-Pad2)
- removed copper zone on B.Cu, net Net-(FL1-Pad4)
- removed copper zone on F.Cu, net Net-(GD1-Pad3)
- removed copper zone on F.Cu, net Net-(J1-Pin_1)
- removed copper zone on F.Cu, net Net-(J2-Pin_1)

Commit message: Added PE keepouts. Adding thermal vias. DRC passing.
Signed-off-by: Jean Alinei <jean.alinei@owntech.org>
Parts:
- moved FID3 236.4 mm to (62.0, 115.5)
- moved FID2 140.5 mm to (204.9, 173.1)
- moved FID1 62.0 mm to (232.0, 52.5)
- moved U901 50.5 mm to (58.1, 115.0)
- moved C28 4.31 mm to (95.4, 149.3), turned to 0 degrees
- moved C39 4.20 mm to (95.3, 158.4), turned to 0 degrees
- moved HS10 0.40 mm to (207.3, 65.6)
- moved HS9 0.28 mm to (207.3, 81.8)
- moved R807 0.26 mm to (213.8, 90.7)
- moved U806 0.26 mm to (211.9, 95.5)
- moved R808 0.26 mm to (213.7, 92.7)
- moved R809 0.26 mm to (210.9, 92.0)
- moved R102 0.25 mm to (204.3, 87.8)
- moved D101 0.25 mm to (208.5, 87.8)
- moved C44 0.10 mm to (98.7, 102.3)
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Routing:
- net /Microcontroller/PWM_{ILow2}: track 107.9 -> 87.7 mm
- net /Microcontroller/PWM_{IHigh2}: track 112.8 -> 93.1 mm
- net DGND: track 57.1 -> 66.6 mm, vias 32 -> 79
- net Earth_Protective: track 55.9 -> 49.3 mm, vias 1 -> 12
- net Net-(C7-Pad2): track 5.49 -> 0.00 mm
- net +5V_{DGND}: track 272.9 -> 277.4 mm, vias 12 -> 19
- net +5V_{HV}: track 126.9 -> 131.0 mm
- net Net-(FL1-Pad4): track 29.4 -> 26.2 mm, vias 1 -> 4
- net +12V_{DGND}: track 175.7 -> 172.8 mm, vias 9 -> 19
- net /Power/AC Current sense/In+: track 46.9 -> 49.5 mm, vias 4 -> 15
- net /Microcontroller/EN_{I}: track 63.7 -> 65.3 mm
- net /Power/HV_{BUS}: track 36.0 -> 34.7 mm, vias 9 -> 24
- net Net-(U702-SW): track 6.93 -> 5.81 mm
- net /Microcontroller/V_{ILow}: track 72.0 -> 70.9 mm
- net /Feeder/DIS_{HV}: track 33.6 -> 33.0 mm
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- added copper zone on B.Cu, net +12V_{DGND}
- added copper zone on In1.Cu, net +12V_{DGND}
- added copper zone on In2.Cu, net +12V_{DGND}
- added copper zone on B.Cu, net +5V_{DGND}
- added copper zone on In1.Cu, net +5V_{DGND}
- added copper zone on In2.Cu, net +5V_{DGND}
- added copper zone on In1.Cu, net /Power/AC Current sense/In+
- added copper zone on In1.Cu, net /Power/Grid Voltage sense/In+
- added copper zone on F.Cu, net Net-(C7-Pad2)
- added copper zone on F.Cu, net Net-(FL1-Pad4)
- added copper zone on In1.Cu, net Net-(FL1-Pad4)
